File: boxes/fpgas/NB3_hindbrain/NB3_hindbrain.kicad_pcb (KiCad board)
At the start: 2 copper layers, 8 parts, among them IC1 NOR_Flash_W25Q32JVSSIQ, IC2 FPGA_ICE40UP5K-SG48I, J1 MicroUSB_10103594-0001LF, U1 USBtoSPI_FT4232HL, U2 EEPROM_93LC56BT-I-OT, Y1 Osc_12MHz_ECS-2520MV-120-BN-TR

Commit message: Tweaks to NB3_hindbrain
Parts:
- added C1: 10uF, Capacitor_SMD:C_0603_1608Metric, F.Cu at (136.1, 74.9)
- added C10: 100nF, Capacitor_SMD:C_0402_1005Metric, B.Cu at (89.9, 79.3)
- added C11: 100nF, Capacitor_SMD:C_0402_1005Metric, B.Cu at (113.0, 81.3)
- added C2: 10uF, Capacitor_SMD:C_0603_1608Metric, F.Cu at (132.1, 81.3)
- added C3: 100nF, Capacitor_SMD:C_0402_1005Metric, B.Cu at (115.9, 83.2)
- added C4: 100nF, Capacitor_SMD:C_0402_1005Metric, B.Cu at (101.6, 81.3)
- added C5: 100nF, Capacitor_SMD:C_0402_1005Metric, B.Cu at (89.9, 81.3)
- added C6: 100nF, Capacitor_SMD:C_0402_1005Metric, B.Cu at (98.7, 81.3)
- added C7: 3.3uF, Capacitor_SMD:C_0603_1608Metric, F.Cu at (136.1, 78.8)
- added C8: 10uF, Capacitor_SMD:C_0603_1608Metric, F.Cu at (132.1, 78.8)
- added C9: 10uF, Capacitor_SMD:C_0603_1608Metric, F.Cu at (132.1, 74.9)
- added J2: Conn_01x20_Male, Connector_PinHeader_2.54mm:PinHeader_1x20_P2.54mm_Vertical, B.Cu at (133.3, 71.1)
- added J3: Conn_01x20_Male, Connector_PinHeader_2.54mm:PinHeader_1x20_P2.54mm_Vertical, B.Cu at (133.3, 88.9)
- added R1: 10k, Resistor_SMD:R_0402_1005Metric, F.Cu at (135.5, 81.0)
- added R2: 10k, Resistor_SMD:R_0402_1005Metric, B.Cu at (98.6, 79.3)
- added R3: 2.2k, Resistor_SMD:R_0402_1005Metric, B.Cu at (92.8, 79.3)
- added R4: 4.7k, Resistor_SMD:R_0402_1005Metric, B.Cu at (115.9, 79.3)
- added R5: 10k, Resistor_SMD:R_0402_1005Metric, B.Cu at (95.7, 79.3)
- added R6: 10k, Resistor_SMD:R_0402_1005Metric, B.Cu at (113.0, 79.3)
- added R7: 1k, Resistor_SMD:R_0402_1005Metric, B.Cu at (101.5, 79.3)
- added R8: 12k, Resistor_SMD:R_0402_1005Metric, F.Cu at (134.6, 85.1)
- IC1: value NOR_Flash_W25Q32JVSSIQ -> FPGA_ICE40UP5K-SG48I; footprint NB3_hindbrain:NOR_Flash_W25Q32JVSSIQ -> NB3_hindbrain:FPGA_ICE40UP5K-SG48I
- IC2: value FPGA_ICE40UP5K-SG48I -> NOR_Flash_W25Q32JVSSIQ; footprint NB3_hindbrain:FPGA_ICE40UP5K-SG48I -> NB3_hindbrain:NOR_Flash_W25Q32JVSSIQ
- VR1: value LDO_1v2_AP7217D-12YG-13 -> LDO_3v3_LM1117IMPX-3.3; footprint NB3_hindbrain:LDO_1v2_AP7217D-12YG-13 -> NB3_hindbrain:LDO_3v3_LM1117IMPX-3.3
- VR2: value LDO_3v3_LM1117IMPX-3.3 -> LDO_1v2_AP7217D-12YG-13; footprint NB3_hindbrain:LDO_3v3_LM1117IMPX-3.3 -> NB3_hindbrain:LDO_1v2_AP7217D-12YG-13
- moved Y1 20.3 mm to (104.1, 86.4)
- moved U2 19.8 mm to (109.2, 86.4)
- moved IC1 11.7 mm to (124.5, 83.8)
- moved VR2 11.3 mm to (115.0, 78.7)
- moved U1 10.1 mm to (92.8, 80.0)
- moved VR1 8.62 mm to (106.7, 78.7)
- moved J1 6.97 mm to (81.3, 80.0)
- moved IC2 5.04 mm to (125.0, 76.2)
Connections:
- net /EEDATA renamed /EEDATA_I
- IC2 pad 2: unconnected-(IC2-Pad2) -> /FPGA_SI
- IC2 pad 4: unconnected-(IC2-Pad4) -> GND
- IC2 pad 5: unconnected-(IC2-Pad5) -> /FPGA_SO
- IC2 pad 6: unconnected-(IC2-Pad6) -> /FPGA_SCK
- IC2 pad 8: unconnected-(IC2-Pad8) -> +3V3
- J1 pad 1: unconnected-(J1-Pad1) -> Net-(J1-Pad1)
- U1 pad 12: unconnected-(U1-Pad12) -> +1V8
- U1 pad 13: unconnected-(U1-Pad13) -> GND
- U1 pad 14: unconnected-(U1-Pad14) -> Net-(R7-Pad2)
- U1 pad 20: unconnected-(U1-Pad20) -> +3V3
- U1 pad 31: unconnected-(U1-Pad31) -> +3V3
- U1 pad 37: unconnected-(U1-Pad37) -> +1V8
- U1 pad 42: unconnected-(U1-Pad42) -> +3V3
- U1 pad 49: unconnected-(U1-Pad49) -> +1V8
- U1 pad 50: unconnected-(U1-Pad50) -> +3V3
- U1 pad 56: unconnected-(U1-Pad56) -> +3V3
- U1 pad 6: unconnected-(U1-Pad6) -> Net-(R8-Pad1)
- U1 pad 64: unconnected-(U1-Pad64) -> +1V8
- U2 pad 1: unconnected-(U2-Pad1) -> /EEDATA_O
- U2 pad 6: unconnected-(U2-Pad6) -> +3V3
- VR1 pad 1: unconnected-(VR1-Pad1) -> GND
- VR1 pad 2: unconnected-(VR1-Pad2) -> +3V3
- VR1 pad 3: unconnected-(VR1-Pad3) -> +5V
- VR1 pad 4: unconnected-(VR1-Pad4) -> +3V3
- VR2 pad 1: unconnected-(VR2-Pad1) -> GND
- VR2 pad 2: unconnected-(VR2-Pad2) -> +5V
- VR2 pad 3: unconnected-(VR2-Pad3) -> +1V2
- VR2 pad 4: unconnected-(VR2-Pad4) -> +5V
- Y1 pad 2: unconnected-(Y1-Pad2) -> GND
- Y1 pad 4: unconnected-(Y1-Pad4) -> +3V3
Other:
- board outline added: 58.4 x 22.9 mm

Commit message: Work on NB3_hindbrain
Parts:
- VR1: moved to B.Cu
- moved VR1 17.8 mm to (88.9, 78.7), turned to 180 degrees
- moved VR2 15.9 mm to (99.1, 78.7), turned to 90 degrees
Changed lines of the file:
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@@
       (net 22 "+3V3") (pinfunction "VCC") (pintype "power_in"))
   )
-  (footprint "NB3_hindbrain:LDO_3v3_LM1117IMPX-3.3" (layer "F.Cu")
-    (at 106.68 78.74)
-    (property "MANUFACTURER" "Texas Instruments")
-    (property "MAXIMUM_PACKAGE_HEIGHT" "1.80 mm")
-    (property "PARTREV" "O")
-    (property "STANDARD" "Manufacturer Recommendation")
-    (property "Sheetfile" "NB3_hindbrain.kicad_sch")
-    (property "Sheetname" "")
-    (attr through_hole)
-    (fp_text reference "VR1" (at -0.025 -4.754) (layer "F.SilkS")
-      (effects (font (size 1 1) (thickness 0.15)))
-    )
-    (fp_text value "LDO_3v3_LM1117IMPX-3.3" (at 11.405 4.365) (layer "F.Fab")
-      (effects (font (size 1 1) (thickness 0.15)))
-    )
-    (fp_line (start 1.75 3.25) (end 1.75 2.01) (layer "F.SilkS") (width 0.127))
-    (fp_line (start -1.75 3.25) (end 1.75 3.25) (layer "F.SilkS") (width 0.127))
-    (fp_line (start 1.75 -3.25) (end 1.75 -2.01) (layer "F.SilkS") (width 0.127))
-    (fp_line (start -1.75 -3.25) (end 1.75 -3.25) (layer "F.SilkS") (width 0.127))
-    (fp_circle (center -4.6 -2.3) (end -4.5 -2.3) (layer "F.SilkS") (width 0.2) (fill none))
-    (fp_line (start 2 -1.875) (end 2 -3.5) (layer "F.CrtYd") (width 0.05))
-    (fp_line (start 2 3.5) (end 2 1.875) (layer "F.CrtYd") (width 0.05))
-    (fp_line (start 4.225 -1.875) (end 2 -1.875) (layer "F.CrtYd") (width 0.05))
-    (fp_line (start 4.225 1.875) (end 4.225 -1.875) (layer "F.CrtYd") (width 0.05))
-    (fp_line (start -2 -3.025) (end -4.225 -3.025) (layer "F.CrtYd") (width 0.05))
-    (fp_line (start -4.225 -3.025) (end -4.225 3.025) (layer "F.CrtYd") (width 0.05))
-    (fp_line (start 2 1.875) (end 4.225 1.875) (layer "F.CrtYd") (width 0.05))
-    (fp_line (start -2 -3.5) (end -2 -3.025) (layer "F.CrtYd") (width 0.05))
-    (fp_line (start -4.225 3.025) (end -2 3.025) (layer "F.CrtYd") (width 0.05))
-    (fp_line (start 2 -3.5) (end -2 -3.5) (layer "F.CrtYd") (width 0.05))
-    (fp_line (start -2 3.5) (end 2 3.5) (layer "F.CrtYd") (width 0.05))
-    (fp_line (start -2 3.025) (end -2 3.5) (layer "F.CrtYd") (width 0.05))
-    (fp_line (start -1.75 -3.25) (end -1.75 3.25) (layer "F.Fab") (width 0.127))
-    (fp_line (start 1.75 3.25) (end -1.75 3.25) (layer "F.Fab") (width 0.127))
-    (fp_line (start 1.75 -3.25) (end 1.75 3.25) (layer "F.Fab") (width 0.127))
-    (fp_line (start 1.75 -3.25) (end -1.75 -3.25) (layer "F.Fab") (width 0.127))
-    (fp_circle (center -4.6 -2.3) (end -4.5 -2.3) (layer "F.Fab") (width 0.2) (fill none))
-    (pad "1" smd rect locked (at -2.9 -2.3) (size 2.15 0.95) (layers "F.Cu" "F.Paste" "F.Mask")
-      (net 16 "GND") (pinfunction "GND") (pintype "power_in"))
-    (pad "2" smd rect locked (at -2.9 0) (size 2.15 0.95) (layers "F.Cu" "F.Paste" "F.Mask")
-      (net 22 "+3V3") (pinfunction "VOUT_2") (pintype "output"))
-    (pad "3" smd rect locked (at -2.9 2.3) (size 2.15 0.95) (layers "F.Cu" "F.Paste" "F.Mask")
-      (net 12 "+5V") (pinfunction "VIN") (pintype "input"))
-    (pad "4" smd rect locked (at 2.9 0) (size 2.15 3.25) (layers "F.Cu" "F.Paste" "F.Mask")
-      (net 22 "+3V3") (pinfunction "VOUT_4") (pintype "output"))
-  )
   (footprint "NB3_hindbrain:LDO_1v2_AP7217D-12YG-13" (layer "F.Cu")
-    (at 115 78.74 -90)
+    (at 99.06 78.74 90)
     (descr "SOT89-3L_1")
     (tags "Integrated Circuit")
@@
     (property "Sheetname" "")
     (attr smd)
-    (fp_text reference "VR2" (at 0 -0.334 -90) (layer "F.SilkS")
+    (fp_text reference "VR2" (at 0 -0.334 90) (layer "F.SilkS")
       (effects (font (size 1.27 1.27) (thickness 0.254)))
     )
-    (fp_text value "LDO_1v2_AP7217D-12YG-13" (at 0 -0.334 -90) (layer "F.SilkS") hide
+    (fp_text value "LDO_1v2_AP7217D-12YG-13" (at 0 -0.334 90) (layer "F.SilkS") hide
       (effects (font (size 1.27 1.27) (thickness 0.254)))
     )
-    (fp_text user "${REFERENCE}" (at 0 -0.334 -90) (layer "F.Fab")
+    (fp_text user "${REFERENCE}" (at 0 -0.334 90) (layer "F.Fab")
       (effects (font (size 1.27 1.27) (thickness 0.254)))
     )
@@
     (fp_line (start 2.25 -1.912) (end 2.25 0.688) (layer "F.Fab") (width 0.2))
     (fp_line (start 2.25 0.688) (end -2.25 0.688) (layer "F.Fab") (width 0.2))
-    (pad "1" smd rect locked (at -1.5 1.25 270) (size 0.9 1.3) (layers "F.Cu" "F.Paste" "F.Mask")
+    (pad "1" smd rect locked (at -1.5 1.25 90) (size 0.9 1.3) (layers "F.Cu" "F.Paste" "F.Mask")
       (net 16 "GND") (pinfunction "GND") (pintype "passive"))
-    (pad "2" smd rect locked (at 0 0.95 270) (size 0.9 1.9) (layers "F.Cu" "F.Paste" "F.Mask")
+    (pad "2" smd rect locked (at 0 0.95 90) (size 0.9 1.9) (layers "F.Cu" "F.Paste" "F.Mask")
       (net 12 "+5V") (pinfunction "VIN_1") (pintype "passive"))
-    (pad "3" smd rect locked (at 1.5 1.25 270) (size 0.9 1.3) (layers "F.Cu" "F.Paste" "F.Mask")
+    (pad "3" smd rect locked (at 1.5 1.25 90) (size 0.9 1.3) (layers "F.Cu" "F.Paste" "F.Mask")
       (net 20 "+1V2") (pinfunction "VOUT") (pintype "passive"))
-    (pad "4" smd rect locked (at 0 -1.35 270) (size 1.733 2.7) (layers "F.Cu" "F.Paste" "F.Mask")
+    (pad "4" smd rect locked (at 0 -1.35 90) (size 1.733 2.7) (layers "F.Cu" "F.Paste" "F.Mask")
       (net 12 "+5V") (pinfunction "VIN_2") (pintype "passive"))
     (model "AP7217D-12YG-13.stp"
@@
     )
   )
+  (footprint "NB3_hindbrain:LDO_3v3_LM1117IMPX-3.3" (layer "B.Cu")
+    (at 88.9 78.74 180)
+    (property "MANUFACTURER" "Texas Instruments")
+    (property "MAXIMUM_PACKAGE_HEIGHT" "1.80 mm")
+    (property "PARTREV" "O")
+    (property "STANDARD" "Manufacturer Recommendation")
+    (property "Sheetfile" "NB3_hindbrain.kicad_sch")
+    (property "Sheetname" "")
+    (attr through_hole)
+    (fp_text reference "VR1" (at -0.025 4.754) (layer "B.SilkS")
+      (effects (font (size 1 1) (thickness 0.15)) (justify mirror))
+    )
+    (fp_text value "LDO_3v3_LM1117IMPX-3.3" (at 11.405 -4.365) (layer "B.Fab")
+      (effects (font (size 1 1) (thickness 0.15)) (justify mirror))
+    )
+    (fp_line (start 1.75 -3.25) (end 1.75 -2.01) (layer "B.SilkS") (width 0.127))
+    (fp_line (start -1.75 -3.25) (end 1.75 -3.25) (layer "B.SilkS") (width 0.127))
+    (fp_line (start 1.75 3.25) (end 1.75 2.01) (layer "B.SilkS") (width 0.127))
+    (fp_line (start -1.75 3.25) (end 1.75 3.25) (layer "B.SilkS") (width 0.127))
+    (fp_circle (center -4.6 2.3) (end -4.5 2.3) (layer "B.SilkS") (width 0.2) (fill none))
+    (fp_line (start 2 1.875) (end 2 3.5) (layer "B.CrtYd") (width 0.05))
+    (fp_line (start 2 -3.5) (end 2 -1.875) (layer "B.CrtYd") (width 0.05))
+    (fp_line (start 4.225 1.875) (end 2 1.875) (layer "B.CrtYd") (width 0.05))
+    (fp_line (start 4.225 -1.875) (end 4.225 1.875) (layer "B.CrtYd") (width 0.05))
+    (fp_line (start -2 3.025) (end -4.225 3.025) (layer "B.CrtYd") (width 0.05))
+    (fp_line (start -4.225 3.025) (end -4.225 -3.025) (layer "B.CrtYd") (width 0.05))
+    (fp_line (start 2 -1.875) (end 4.225 -1.875) (layer "B.CrtYd") (width 0.05))
+    (fp_line (start -2 3.5) (end -2 3.025) (layer "B.CrtYd") (width 0.05))
+    (fp_line (start -4.225 -3.025) (end -2 -3.025) (layer "B.CrtYd") (width 0.05))
+    (fp_line (start 2 3.5) (end -2 3.5) (layer "B.CrtYd") (width 0.05))
+    (fp_line (start -2 -3.5) (end 2 -3.5) (layer "B.CrtYd") (width 0.05))
+    (fp_line (start -2 -3.025) (end -2 -3.5) (layer "B.CrtYd") (width 0.05))
+    (fp_line (start -1.75 3.25) (end -1.75 -3.25) (layer "B.Fab") (width 0.127))
+    (fp_line (start 1.75 -3.25) (end -1.75 -3.25) (layer "B.Fab") (width 0.127))
+    (fp_line (start 1.75 3.25) (end 1.75 -3.25) (layer "B.Fab") (width 0.127))
+    (fp_line (start 1.75 3.25) (end -1.75 3.25) (layer "B.Fab") (width 0.127))
+    (fp_circle (center -4.6 2.3) (end -4.5 2.3) (layer "B.Fab") (width 0.2) (fill none))
+    (pad "1" smd rect locked (at -2.9 2.3 180) (size 2.15 0.95) (layers "B.Cu" "B.Paste" "B.Mask")
+      (net 16 "GND") (pinfunction "GND") (pintype "power_in"))
+    (pad "2" smd rect locked (at -2.9 0 180) (size 2.15 0.95) (layers "B.Cu" "B.Paste" "B.Mask")
+      (net 22 "+3V3") (pinfunction "VOUT_2") (pintype "output"))
+    (pad "3" smd rect locked (at -2.9 -2.3 180) (size 2.15 0.95) (layers "B.Cu" "B.Paste" "B.Mask")
+      (net 12 "+5V") (pinfunction "VIN") (pintype "input"))
+    (pad "4" smd rect locked (at 2.9 0 180) (size 2.15 3.25) (layers "B.Cu" "B.Paste" "B.Mask")
+      (net 22 "+3V3") (pinfunction "VOUT_4") (pintype "output"))
+  )
   (footprint "Connector_PinHeader_2.54mm:PinHeader_1x20_P2.54mm_Vertical" (layer "B.Cu")

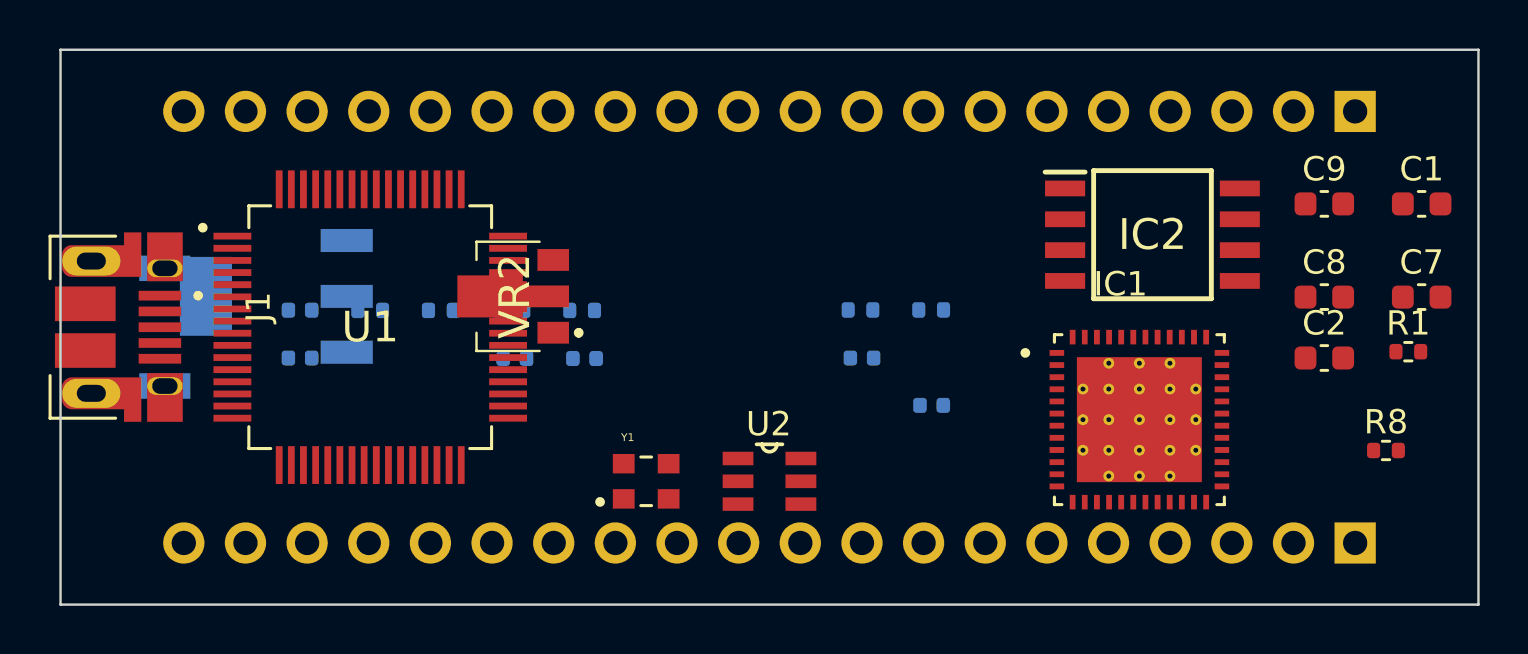
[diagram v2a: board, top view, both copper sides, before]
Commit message: Update NB3_hindbrain (3D models)
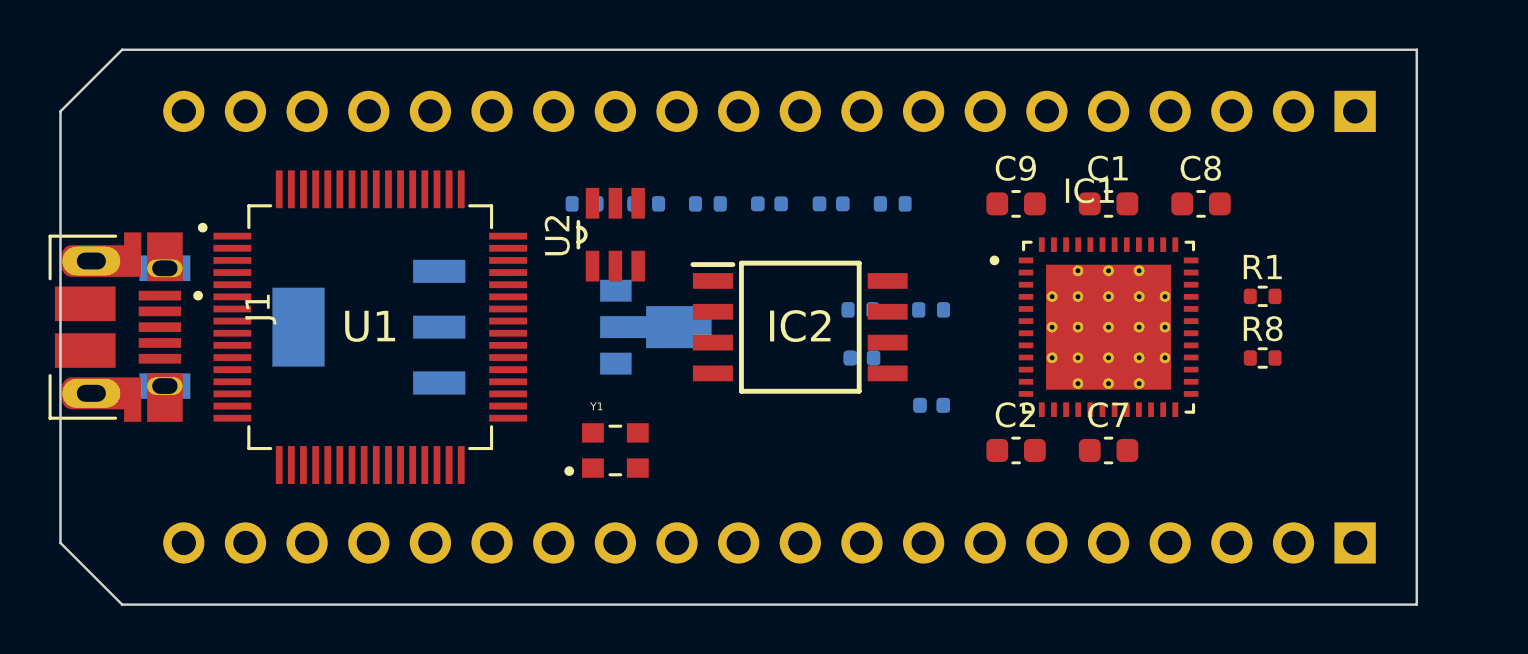
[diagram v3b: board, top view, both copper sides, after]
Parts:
- VR2: moved to B.Cu
- moved IC2 15.0 mm to (110.5, 80.0)
- moved C6 14.5 mm to (111.8, 74.9)
- moved C7 14.4 mm to (123.2, 85.1)
- moved R7 13.5 mm to (114.3, 74.9)
- moved C2 13.3 mm to (119.4, 85.1)
- moved C1 12.9 mm to (123.2, 74.9)
- moved C9 12.7 mm to (119.4, 74.9)
- moved U2 12.0 mm to (102.9, 76.2), turned to 90 degrees
- moved C4 9.93 mm to (109.2, 74.9)
- moved R3 9.86 mm to (101.6, 74.9)
- moved R5 9.53 mm to (104.1, 74.9)
- moved R2 9.20 mm to (106.7, 74.9)
- moved R1 6.42 mm to (129.5, 78.7)
- moved C8 6.37 mm to (127.0, 74.9)
- moved R8 6.35 mm to (129.5, 81.3)
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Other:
- board size 58.4 x 22.9 mm -> 55.9 x 22.9 mm
